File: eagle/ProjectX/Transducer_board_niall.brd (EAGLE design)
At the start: 100 x 100 mm, 104 parts, among them T1 MA40S4S, T10 MA40S4S, T100 MA40S4S, T11 MA40S4S, T12 MA40S4S, T13 MA40S4S, T14 MA40S4S, T15 MA40S4S, T16 MA40S4S, T17 MA40S4S, T18 MA40S4S, T19 MA40S4S, T2 MA40S4S, T20 MA40S4S, T21 MA40S4S, T22 MA40S4S, T23 MA40S4S, T24 MA40S4S, T25 MA40S4S, T26 MA40S4S, T27 MA40S4S, T28 MA40S4S, T29 MA40S4S, T3 MA40S4S, T30 MA40S4S, T31 MA40S4S, T32 MA40S4S, T33 MA40S4S, T34 MA40S4S, T35 MA40S4S, T36 MA40S4S, T37 MA40S4S, T38 MA40S4S, T39 MA40S4S, T4 MA40S4S, T40 MA40S4S, T41 MA40S4S, T42 MA40S4S, T43 MA40S4S, T44 MA40S4S, T45 MA40S4S, T46 MA40S4S, T47 MA40S4S, T48 MA40S4S, T49 MA40S4S, T5 MA40S4S, T50 MA40S4S, T51 MA40S4S, T52 MA40S4S, T53 MA40S4S, T54 MA40S4S, T55 MA40S4S, T56 MA40S4S, T57 MA40S4S, T58 MA40S4S, T59 MA40S4S, T6 MA40S4S, T60 MA40S4S, T61 MA40S4S, T62 MA40S4S, T63 MA40S4S, T64 MA40S4S, T65 MA40S4S, T66 MA40S4S, T67 MA40S4S, T68 MA40S4S, T69 MA40S4S, T7 MA40S4S, T70 MA40S4S, T71 MA40S4S, T72 MA40S4S, T73 MA40S4S, T74 MA40S4S, T75 MA40S4S, T76 MA40S4S, T77 MA40S4S, T78 MA40S4S, T79 MA40S4S, T8 MA40S4S, T80 MA40S4S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

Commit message: Transducer board small changes
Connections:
- new net TEMP10: 3.34
- new net TEMP11: 3.32
- new net TEMP12: 3.30
- new net TEMP13: 3.28
- new net TEMP14: 3.26
- new net TEMP15: 3.24
- new net TEMP16: 3.22
- new net TEMP17: 3.20
- new net TEMP18: 3.18
- new net TEMP19: 3.16
- new net TEMP2: 3.50
- new net TEMP20: 3.14
- new net TEMP21: 3.12
- new net TEMP22: 3.8
- new net TEMP23: 3.6
- new net TEMP24: 3.4
- new net TEMP25: 3.2
- new net TEMP26: 3.10
- new net TEMP27: 3.1
- new net TEMP28: 3.3
- new net TEMP29: 3.5
- new net TEMP3: 3.48
- new net TEMP30: 3.7
- new net TEMP31: 3.9
- new net TEMP32: 3.11
- new net TEMP33: 3.13
- new net TEMP34: 3.15
- new net TEMP35: 3.17
- new net TEMP36: 3.19
- new net TEMP37: 3.21
- new net TEMP38: 3.23
- new net TEMP39: 3.25
- new net TEMP4: 3.46
- new net TEMP40: 3.27
- new net TEMP41: 3.29
- new net TEMP42: 3.31
- new net TEMP43: 3.33
- new net TEMP44: 3.35
- new net TEMP45: 3.37
- new net TEMP46: 3.39
- new net TEMP47: 3.41
- new net TEMP48: 3.43
- new net TEMP49: 3.45
- new net TEMP5: 3.44
- new net TEMP50: 3.47
- new net TEMP51: 3.49
- new net TEMP6: 3.42
- new net TEMP7: 3.40
- new net TEMP8: 3.38
- new net TEMP9: 3.36
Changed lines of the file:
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@@
 <wire x1="21.4144" y1="17.9" x2="21.2874" y2="17.773" width="0.2032" layer="16"/>
+</signal>
+<signal name="TEMP2">
+<contactref element="3" pad="50"/>
+</signal>
+<signal name="TEMP3">
+<contactref element="3" pad="48"/>
+</signal>
+<signal name="TEMP4">
+<contactref element="3" pad="46"/>
+</signal>
+<signal name="TEMP5">
+<contactref element="3" pad="44"/>
+</signal>
+<signal name="TEMP6">
+<contactref element="3" pad="42"/>
+</signal>
+<signal name="TEMP7">
+<contactref element="3" pad="40"/>
+</signal>
+<signal name="TEMP8">
+<contactref element="3" pad="38"/>
+</signal>
+<signal name="TEMP9">
+<contactref element="3" pad="36"/>
+</signal>
+<signal name="TEMP10">
+<contactref element="3" pad="34"/>
+</signal>
+<signal name="TEMP11">
+<contactref element="3" pad="32"/>
+</signal>
+<signal name="TEMP12">
+<contactref element="3" pad="30"/>
+</signal>
+<signal name="TEMP13">
+<contactref element="3" pad="28"/>
+</signal>
+<signal name="TEMP14">
+<contactref element="3" pad="26"/>
+</signal>
+<signal name="TEMP15">
+<contactref element="3" pad="24"/>
+</signal>
+<signal name="TEMP16">
+<contactref element="3" pad="22"/>
+</signal>
+<signal name="TEMP17">
+<contactref element="3" pad="20"/>
+</signal>
+<signal name="TEMP18">
+<contactref element="3" pad="18"/>
+</signal>
+<signal name="TEMP19">
+<contactref element="3" pad="16"/>
+</signal>
+<signal name="TEMP20">
+<contactref element="3" pad="14"/>
+</signal>
+<signal name="TEMP21">
+<contactref element="3" pad="12"/>
+</signal>
+<signal name="TEMP22">
+<contactref element="3" pad="8"/>
+</signal>
+<signal name="TEMP23">
+<contactref element="3" pad="6"/>
+</signal>
+<signal name="TEMP24">
+<contactref element="3" pad="4"/>
+</signal>
+<signal name="TEMP25">
+<contactref element="3" pad="2"/>
+</signal>
+<signal name="TEMP26">
+<contactref element="3" pad="10"/>
+</signal>
+<signal name="TEMP27">
+<contactref element="3" pad="1"/>
+</signal>
+<signal name="TEMP28">
+<contactref element="3" pad="3"/>
+</signal>
+<signal name="TEMP29">
+<contactref element="3" pad="5"/>
+</signal>
+<signal name="TEMP30">
+<contactref element="3" pad="7"/>
+</signal>
+<signal name="TEMP31">
+<contactref element="3" pad="9"/>
+</signal>
+<signal name="TEMP32">
+<contactref element="3" pad="11"/>
+</signal>
+<signal name="TEMP33">
+<contactref element="3" pad="13"/>
+</signal>
+<signal name="TEMP34">
+<contactref element="3" pad="15"/>
+</signal>
+<signal name="TEMP35">
+<contactref element="3" pad="17"/>
+</signal>
+<signal name="TEMP36">
+<contactref element="3" pad="19"/>
+</signal>
+<signal name="TEMP37">
+<contactref element="3" pad="21"/>
+</signal>
+<signal name="TEMP38">
+<contactref element="3" pad="23"/>
+</signal>
+<signal name="TEMP39">
+<contactref element="3" pad="25"/>
+</signal>
+<signal name="TEMP40">
+<contactref element="3" pad="27"/>
+</signal>
+<signal name="TEMP41">
+<contactref element="3" pad="29"/>
+</signal>
+<signal name="TEMP42">
+<contactref element="3" pad="31"/>
+</signal>
+<signal name="TEMP43">
+<contactref element="3" pad="33"/>
+</signal>
+<signal name="TEMP44">
+<contactref element="3" pad="35"/>
+</signal>
+<signal name="TEMP45">
+<contactref element="3" pad="37"/>
+</signal>
+<signal name="TEMP46">
+<contactref element="3" pad="39"/>
+</signal>
+<signal name="TEMP47">
+<contactref element="3" pad="41"/>
+</signal>
+<signal name="TEMP48">
+<contactref element="3" pad="43"/>
+</signal>
+<signal name="TEMP49">
+<contactref element="3" pad="45"/>
+</signal>
+<signal name="TEMP50">
+<contactref element="3" pad="47"/>
+</signal>
+<signal name="TEMP51">
+<contactref element="3" pad="49"/>
 </signal>
 </signals>

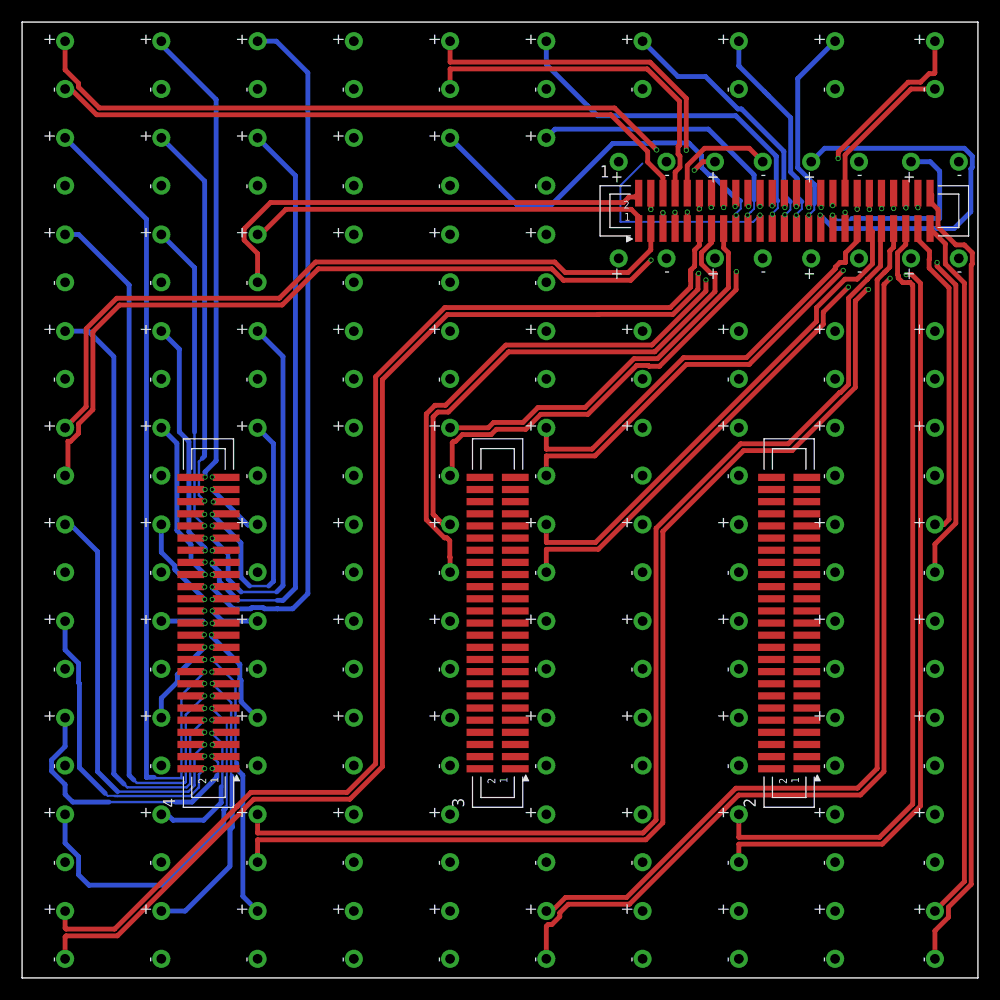
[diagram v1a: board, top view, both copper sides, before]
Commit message: Niall driver board finished draft 1
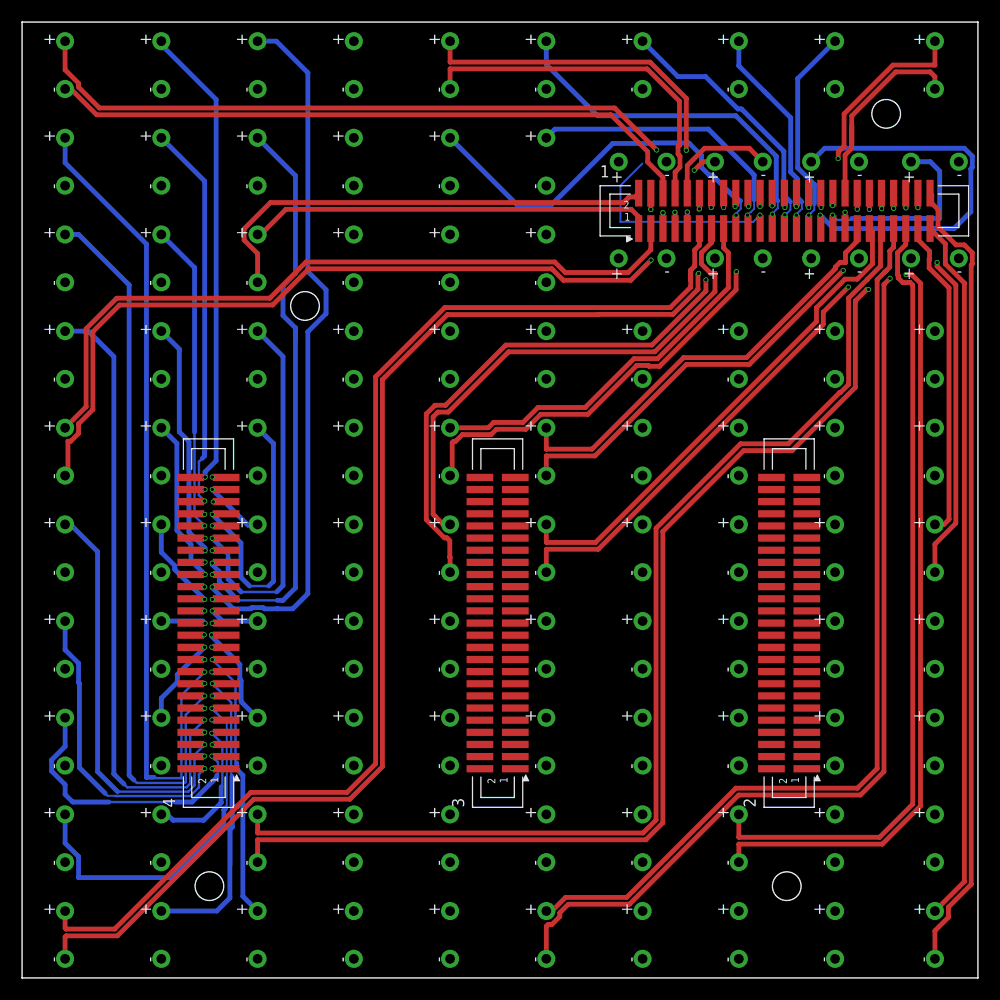
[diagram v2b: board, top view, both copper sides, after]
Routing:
- net FROM_T_9: track 143.8 -> 86.2 mm
- net FROM_T_91: track 16.3 -> 22.4 mm
- net TO_T_29: track 61.8 -> 63.8 mm
- net FROM_T_20: track 34.9 -> 36.8 mm
- net TO_T_20: track 39.9 -> 41.9 mm
- net FROM_T_30: track 70.0 -> 71.6 mm
- net TO_T_30: track 74.3 -> 75.9 mm
- net TO_T_91: track 25.5 -> 27.0 mm
- net FROM_T_29: track 57.4 -> 58.5 mm

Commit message: Niall almost done
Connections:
- new net TEMP100: 2.47
- new net TEMP101: 2.49
- new net TEMP52: 2.50
- new net TEMP53: 2.48
- new net TEMP54: 2.46
- new net TEMP55: 2.44
- new net TEMP56: 2.42
- new net TEMP57: 2.40
- new net TEMP58: 2.38
- new net TEMP59: 2.36
- new net TEMP60: 2.34
- new net TEMP61: 2.32
- new net TEMP62: 2.30
- new net TEMP63: 2.28
- new net TEMP64: 2.26
- new net TEMP65: 2.24
- new net TEMP66: 2.22
- new net TEMP67: 2.20
- new net TEMP68: 2.18
- new net TEMP69: 2.16
- new net TEMP70: 2.14
- new net TEMP71: 2.12
- new net TEMP72: 2.10
- new net TEMP73: 2.8
- new net TEMP74: 2.6
- new net TEMP75: 2.4
- new net TEMP76: 2.2
- new net TEMP77: 2.1
- new net TEMP78: 2.3
- new net TEMP79: 2.5
- new net TEMP80: 2.7
- new net TEMP81: 2.9
- new net TEMP82: 2.11
- new net TEMP83: 2.13
- new net TEMP84: 2.15
- new net TEMP85: 2.17
- new net TEMP86: 2.19
- new net TEMP87: 2.21
- new net TEMP88: 2.23
- new net TEMP89: 2.25
- new net TEMP90: 2.27
- new net TEMP91: 2.29
- new net TEMP92: 2.31
- new net TEMP93: 2.33
- new net TEMP94: 2.35
- new net TEMP95: 2.37
- new net TEMP96: 2.39
- new net TEMP97: 2.41
- new net TEMP98: 2.43
- new net TEMP99: 2.45
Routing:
- net TEMP42: track 0.00 -> 22.8 mm, vias 0 -> 1
- net TEMP11: track 0.00 -> 22.7 mm, vias 0 -> 1
- net TEMP41: track 0.00 -> 21.5 mm, vias 0 -> 1
- net TEMP12: track 0.00 -> 21.5 mm, vias 0 -> 1
- net TEMP40: track 0.00 -> 20.1 mm, vias 0 -> 1
- net TEMP13: track 0.00 -> 20.0 mm, vias 0 -> 1
- net TEMP39: track 0.00 -> 18.8 mm, vias 0 -> 1
- net TEMP14: track 0.00 -> 18.8 mm, vias 0 -> 1
- net TEMP15: track 0.00 -> 17.3 mm, vias 0 -> 1
- net TEMP38: track 0.00 -> 17.3 mm, vias 0 -> 1
- net TEMP37: track 0.00 -> 16.2 mm, vias 0 -> 1
- net TEMP16: track 0.00 -> 15.9 mm, vias 0 -> 1
- net TEMP36: track 0.00 -> 14.7 mm, vias 0 -> 1
- net TEMP17: track 0.00 -> 14.5 mm, vias 0 -> 1
- net TEMP35: track 0.00 -> 13.5 mm, vias 0 -> 1
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
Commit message: Transducer board in finished state
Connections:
- removed net TEMP10: 3.34
- removed net TEMP100: 2.47
- removed net TEMP101: 2.49
- removed net TEMP11: 3.32
- removed net TEMP12: 3.30
- removed net TEMP13: 3.28
- removed net TEMP14: 3.26
- removed net TEMP15: 3.24
- removed net TEMP16: 3.22
- removed net TEMP17: 3.20
- removed net TEMP18: 3.18
- removed net TEMP19: 3.16
- removed net TEMP2: 3.50
- removed net TEMP20: 3.14
- removed net TEMP21: 3.12
- removed net TEMP22: 3.8
- removed net TEMP23: 3.6
- removed net TEMP24: 3.4
- removed net TEMP25: 3.2
- removed net TEMP26: 3.10
- removed net TEMP27: 3.1
- removed net TEMP28: 3.3
- removed net TEMP29: 3.5
- removed net TEMP3: 3.48
- removed net TEMP30: 3.7
- removed net TEMP31: 3.9
- removed net TEMP32: 3.11
- removed net TEMP33: 3.13
- removed net TEMP34: 3.15
- removed net TEMP35: 3.17
- removed net TEMP36: 3.19
- removed net TEMP37: 3.21
- removed net TEMP38: 3.23
- removed net TEMP39: 3.25
- removed net TEMP4: 3.46
- removed net TEMP40: 3.27
- removed net TEMP41: 3.29
- removed net TEMP42: 3.31
- removed net TEMP43: 3.33
- removed net TEMP44: 3.35
- removed net TEMP45: 3.37
- removed net TEMP46: 3.39
- removed net TEMP47: 3.41
- removed net TEMP48: 3.43
- removed net TEMP49: 3.45
- removed net TEMP5: 3.44
- removed net TEMP50: 3.47
- removed net TEMP51: 3.49
- removed net TEMP52: 2.50
- removed net TEMP53: 2.48
- removed net TEMP54: 2.46
- removed net TEMP55: 2.44
- removed net TEMP56: 2.42
- removed net TEMP57: 2.40
- removed net TEMP58: 2.38
- removed net TEMP59: 2.36
- removed net TEMP6: 3.42
- removed net TEMP60: 2.34
- removed net TEMP61: 2.32
- removed net TEMP62: 2.30
- removed net TEMP63: 2.28
- removed net TEMP64: 2.26
- removed net TEMP65: 2.24
- removed net TEMP66: 2.22
- removed net TEMP67: 2.20
- removed net TEMP68: 2.18
- removed net TEMP69: 2.16
- removed net TEMP7: 3.40
- removed net TEMP70: 2.14
- removed net TEMP71: 2.12
- removed net TEMP72: 2.10
- removed net TEMP73: 2.8
- removed net TEMP74: 2.6
- removed net TEMP75: 2.4
- removed net TEMP76: 2.2
- removed net TEMP77: 2.1
- removed net TEMP78: 2.3
- removed net TEMP79: 2.5
- removed net TEMP8: 3.38
- removed net TEMP80: 2.7
- removed net TEMP81: 2.9
- removed net TEMP82: 2.11
- removed net TEMP83: 2.13
- removed net TEMP84: 2.15
- removed net TEMP85: 2.17
- removed net TEMP86: 2.19
- removed net TEMP87: 2.21
- removed net TEMP88: 2.23
- removed net TEMP89: 2.25
- removed net TEMP9: 3.36
- removed net TEMP90: 2.27
- removed net TEMP91: 2.29
- removed net TEMP92: 2.31
- removed net TEMP93: 2.33
- removed net TEMP94: 2.35
- removed net TEMP95: 2.37
- removed net TEMP96: 2.39
- removed net TEMP97: 2.41
- removed net TEMP98: 2.43
- removed net TEMP99: 2.45
- net FROM_T_31: now also 3.48
- net FROM_T_32: now also 3.44
- net FROM_T_33: now also 3.36
- net FROM_T_34: now also 3.32
- net FROM_T_35: now also 3.20
- net FROM_T_36: now also 3.16
- net FROM_T_37: now also 3.12
- net FROM_T_38: now also 3.8
- net FROM_T_39: now also 3.4
- net FROM_T_40: now also 3.5
- net FROM_T_41: now also 3.9
- net FROM_T_42: now also 3.1
- net FROM_T_43: now also 3.24
- net FROM_T_44: now also 3.28
- net FROM_T_47: now also 3.40
- net FROM_T_48: now also 3.49
- net FROM_T_53: now also 3.45
- net FROM_T_54: now also 3.41
- net FROM_T_57: now also 3.21
- net FROM_T_58: now also 3.17
- net FROM_T_59: now also 3.13
- net FROM_T_61: now also 2.8
- net FROM_T_62: now also 2.12
- net FROM_T_63: now also 2.16
- net FROM_T_64: now also 2.20
- net FROM_T_65: now also 3.25
- net FROM_T_66: now also 3.29
- net FROM_T_67: now also 3.33
- net FROM_T_68: now also 3.37
- net FROM_T_73: now also 2.44
- net FROM_T_74: now also 2.40
- net FROM_T_75: now also 2.36
- net FROM_T_76: now also 2.32
- net FROM_T_77: now also 2.28
- net FROM_T_78: now also 2.24
- net FROM_T_80: now also 2.4
- net FROM_T_81: now also 2.1
- net FROM_T_82: now also 2.9
- net FROM_T_83: now also 2.25
- net FROM_T_84: now also 2.21
- net FROM_T_85: now also 2.29
- net FROM_T_86: now also 2.37
- net FROM_T_87: now also 2.45
- net FROM_T_88: now also 2.48
- net FROM_T_93: now also 2.49
- net FROM_T_94: now also 2.41
- net FROM_T_95: now also 2.33
- net FROM_T_97: now also 2.17
- net FROM_T_98: now also 2.13
- net FROM_T_99: now also 2.5
- net TO_T_31: now also 3.46
- net TO_T_32: now also 3.42
- net TO_T_33: now also 3.34
- net TO_T_34: now also 3.30
- net TO_T_35: now also 3.18
- net TO_T_36: now also 3.14
- net TO_T_37: now also 3.10
- net TO_T_38: now also 3.6
- net TO_T_39: now also 3.2
- net TO_T_40: now also 3.7
- net TO_T_41: now also 3.11
- net TO_T_42: now also 3.3
- net TO_T_43: now also 3.22
- net TO_T_44: now also 3.26
- net TO_T_47: now also 3.38
- net TO_T_48: now also 3.50
- net TO_T_53: now also 3.47
- net TO_T_54: now also 3.43
- net TO_T_57: now also 3.23
- net TO_T_58: now also 3.19
- net TO_T_59: now also 3.15
- net TO_T_61: now also 2.6
- net TO_T_62: now also 2.10
- net TO_T_63: now also 2.14
- net TO_T_64: now also 2.18
- net TO_T_65: now also 3.27
- net TO_T_66: now also 3.31
- net TO_T_67: now also 3.35
- net TO_T_68: now also 3.39
- net TO_T_73: now also 2.42
- net TO_T_74: now also 2.38
- net TO_T_75: now also 2.34
- net TO_T_76: now also 2.30
- net TO_T_77: now also 2.26
- net TO_T_78: now also 2.22
- net TO_T_80: now also 2.2
- net TO_T_81: now also 2.3
- net TO_T_82: now also 2.11
- net TO_T_83: now also 2.27
- net TO_T_84: now also 2.23
- net TO_T_85: now also 2.31
- net TO_T_86: now also 2.39
- net TO_T_87: now also 2.47
- net TO_T_88: now also 2.46
- net TO_T_93: now also 2.50
- net TO_T_94: now also 2.43
- net TO_T_95: now also 2.35
- net TO_T_97: now also 2.19
- net TO_T_98: now also 2.15
- net TO_T_99: now also 2.7
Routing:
- net TO_T_35: track 0.00 -> 56.2 mm, vias 0 -> 1
- net TO_T_31: track 0.00 -> 55.8 mm, vias 0 -> 1
- net FROM_T_35: track 0.00 -> 54.4 mm, vias 0 -> 1
- net FROM_T_31: track 0.00 -> 52.5 mm, vias 0 -> 1
- net TO_T_32: track 0.00 -> 48.2 mm, vias 0 -> 1
- net TO_T_36: track 0.00 -> 46.4 mm, vias 0 -> 1
- net FROM_T_32: track 0.00 -> 43.8 mm, vias 0 -> 1
- net TO_T_33: track 0.00 -> 43.5 mm, vias 0 -> 1
- net FROM_T_68: track 0.00 -> 42.6 mm, vias 0 -> 1
- net FROM_T_36: track 0.00 -> 42.3 mm, vias 0 -> 1
- net TO_T_97: track 0.00 -> 41.0 mm, vias 0 -> 1
- net TO_T_84: track 0.00 -> 39.0 mm, vias 0 -> 1
- net TO_T_34: track 0.00 -> 37.9 mm, vias 0 -> 1
- net FROM_T_33: track 0.00 -> 37.8 mm, vias 0 -> 1
- net FROM_T_93: track 0.00 -> 36.5 mm, vias 0 -> 1
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- added copper zone on layer 2, net SHIELD

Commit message: Transducer board in finished state
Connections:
- removed net FROM_T_11: 4.49, T11.-
- new net SHIELD: 4.49
- net FROM_T_12: now also T11.-
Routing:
- net FROM_T_12: track 38.1 -> 85.5 mm
- net FROM_T_11: track 47.3 -> 0.00 mm, vias 1 -> 0
- net TO_T_61: track 29.3 -> 27.7 mm
- net FROM_T_61: track 34.7 -> 33.1 mm
- net FROM_T_63: track 25.4 -> 26.4 mm
- net SHIELD: track 0.00 -> 0.91 mm, vias 0 -> 1
- net TO_T_63: track 27.4 -> 28.0 mm

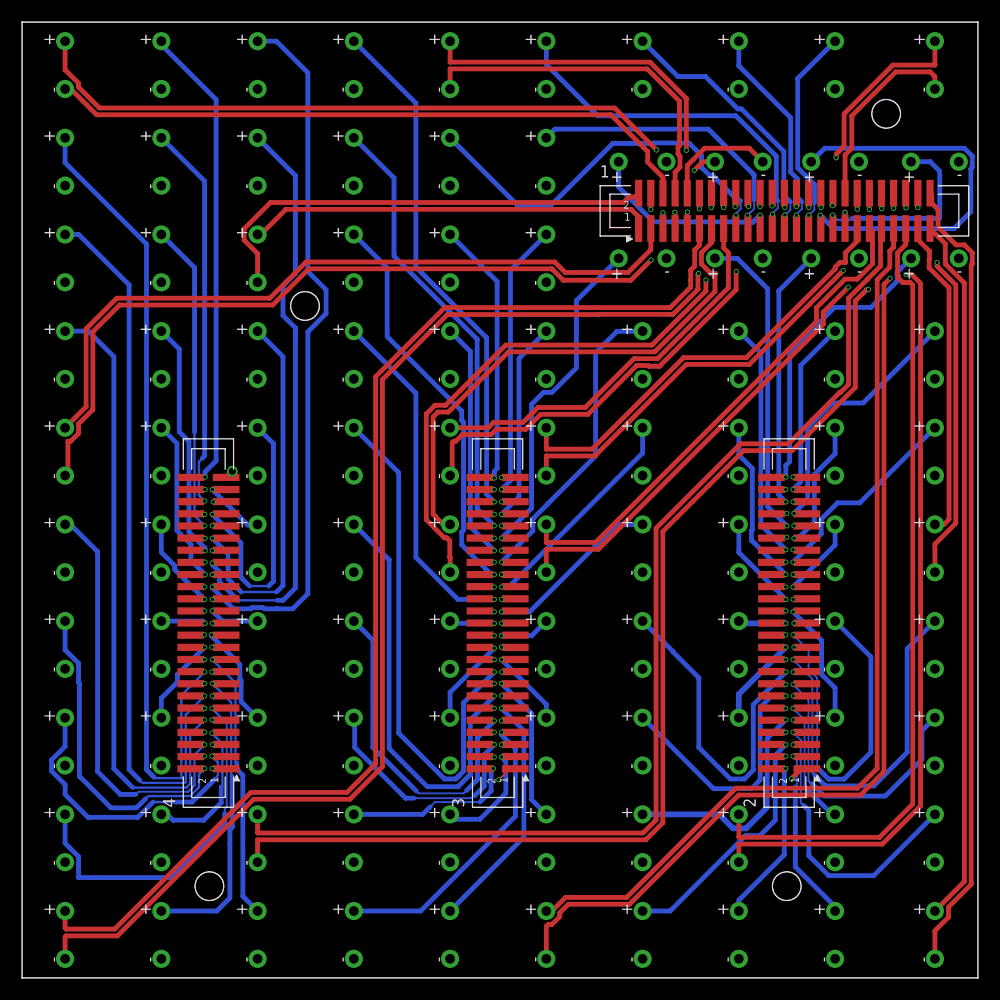
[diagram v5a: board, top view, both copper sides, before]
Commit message: New transducer numbering start
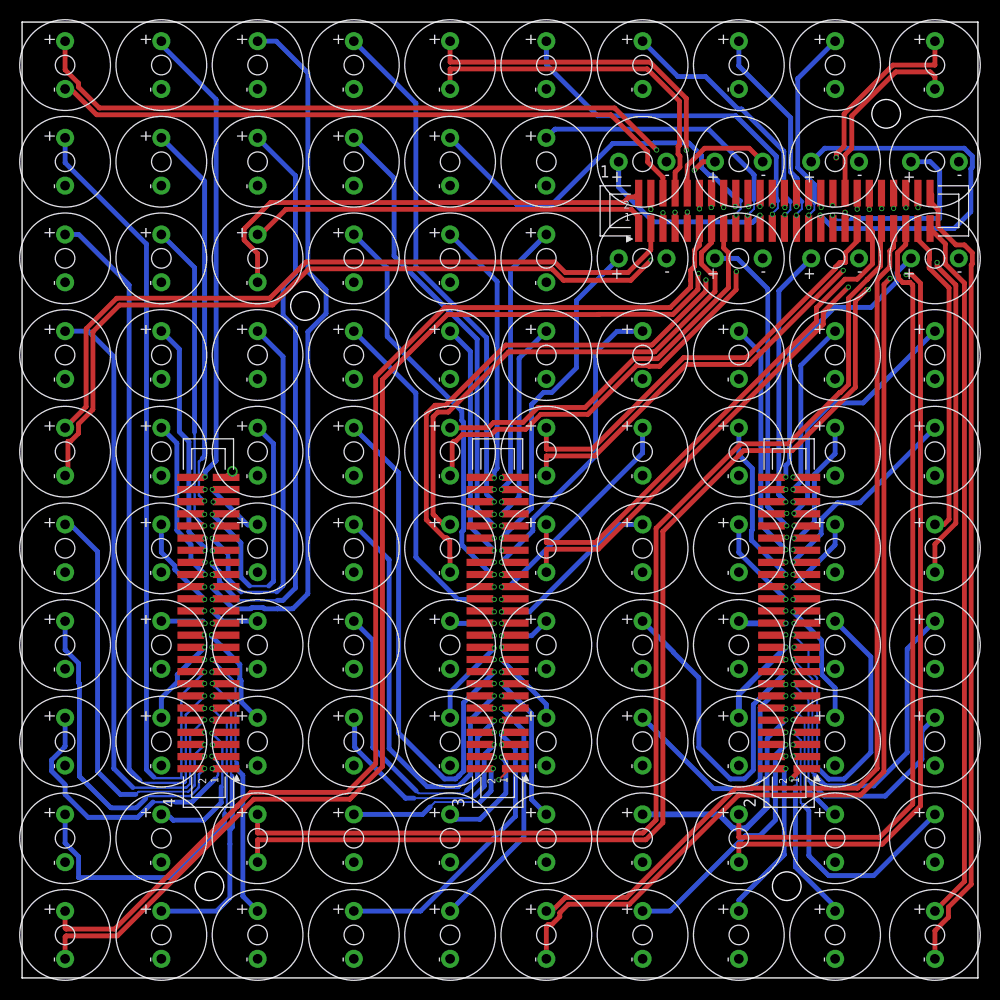
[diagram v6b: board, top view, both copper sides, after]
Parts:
- renumbered T1 to T_19, T10 to T_22, T100 to T_00, T22 to T_04, T28 to T_24, T31 to T_52, T32 to T_54, T33 to T_58, T34 to T_60, T44 to T_62, T45 to T_18, T46 to T_17, T47 to T_56, T48 to T_50, T49 to T_16, T50 to T_21, T51 to T_13, T52 to T_15, T53 to T_51, T54 to T_53, T55 to T_06, T56 to T_05, T6 to T_23, T60 to T_03, T61 to T_47, T62 to T_45, T63 to T_43, T64 to T_41, T65 to T_61, T66 to T_59, T67 to T_57, T68 to T_55, T69 to T_14, T70 to T_12, T71 to T_11, T72 to T_20, T73 to T_29, T74 to T_31, T75 to T_33, T76 to T_35, T77 to T_37, T78 to T_39, T79 to T_02, T80 to T_49, T81 to T_48, T82 to T_44, T83 to T_36, T84 to T_38, T85 to T_34, T86 to T_30, T87 to T_26, T88 to T_27, T89 to T_09, T90 to T_10, T91 to T_07, T92 to T_08, T93 to T_25, T94 to T_28, T95 to T_32, T96 to T_01, T97 to T_40, T98 to T_42, T99 to T_46

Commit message: Boards almost done
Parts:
- renumbered T11 to T_75, T12 to T_77, T13 to T_79, T14 to T_81, T15 to T_83, T16 to T_85, T17 to T_87, T18 to T_89, T19 to T_96, T2 to T_94, T20 to T_92, T21 to T_90, T23 to T_88, T24 to T_86, T25 to T_76, T26 to T_78, T27 to T_80, T29 to T_82, T3 to T_98, T30 to T_84, T35 to T_66, T36 to T_68, T37 to T_70, T38 to T_72, T39 to T_74, T4 to T_99, T40 to T_71, T41 to T_69, T42 to T_73, T43 to T_64, T5 to T_97, T57 to T_63, T58 to T_65, T59 to T_67, T7 to T_95, T8 to T_93, T9 to T_91

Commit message: Version 0 Niall's boards finished design... maybe
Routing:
- net FROM_T_12: track 85.5 -> 89.6 mm
- net TO_T_12: track 41.8 -> 43.9 mm
- net TO_T_29: track 63.8 -> 61.8 mm
- net TO_T_11: track 50.0 -> 51.9 mm
- net FROM_T_30: track 71.1 -> 69.5 mm
- net TO_T_30: track 75.9 -> 74.3 mm
- net FROM_T_2: track 33.4 -> 34.5 mm
- net FROM_T_29: track 58.5 -> 57.4 mm
